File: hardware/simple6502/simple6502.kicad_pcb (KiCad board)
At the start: 2 copper layers, 100 x 100 mm, 41 parts, among them J1 ~{VP}, J2 CLK SEL, J3 RESET, J4 GND, J5 POWER 5V, J6 AUX 5VDC, SW1 RESET, SW2 POWER, T1 DS1813-10+, U1 W65C02SxP, U2 RAM 62256, U3 ROM 28C256, U4 74LS30, U5 74HCT00, U6 74HC138, U7 74HCT273, X1 ACO-1MHz

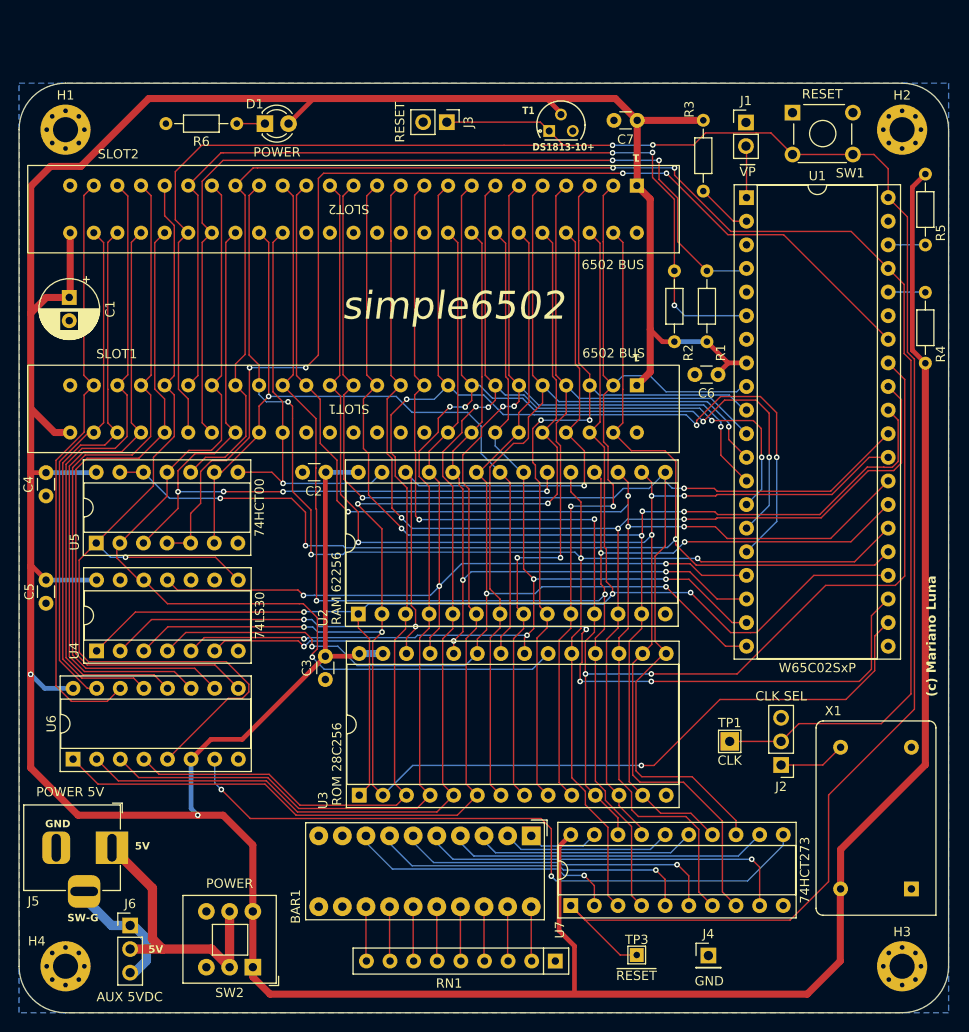
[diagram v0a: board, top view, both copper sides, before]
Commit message: new all in one design with ACIA 68B50
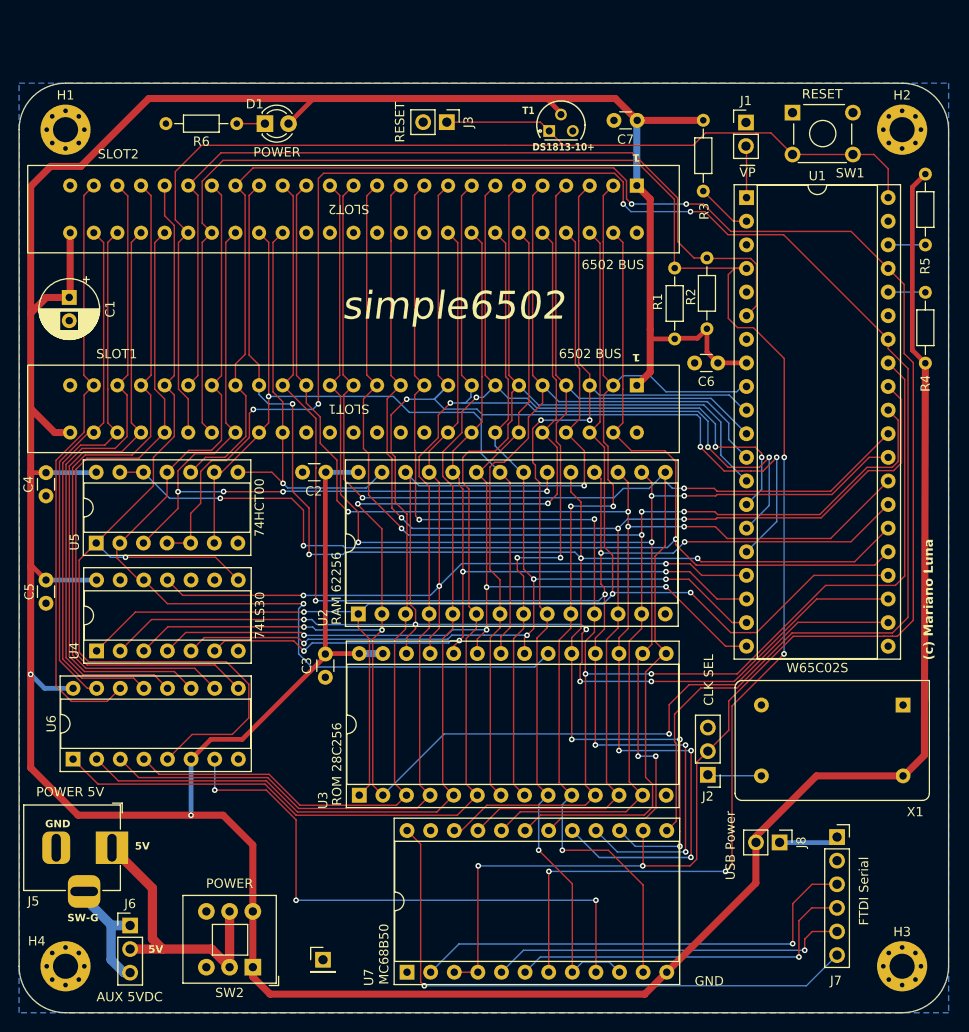
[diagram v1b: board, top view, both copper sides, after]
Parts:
- removed BAR1: HDSP-4850_2, Display:HDSP-4850
- removed RN1: R_Network08_US, Resistor_THT:R_Array_SIP9
- removed TP1: CLK, TestPoint:TestPoint_THTPad_2.0x2.0mm_Drill1.0mm
- removed TP3: ~{RESET}, TestPoint:TestPoint_THTPad_1.5x1.5mm_Drill0.7mm
- added J7: FTDI Serial, Connector_PinSocket_2.54mm:PinSocket_1x06_P2.54mm_Vertical, F.Cu at (138.0, 131.1)
- added J8: USB Power, Connector_PinHeader_2.54mm:PinHeader_1x02_P2.54mm_Vertical, F.Cu at (131.8, 131.7)
- U1: value W65C02SxP -> W65C02S
- U7: value 74HCT273 -> MC68B50; footprint Package_DIP:DIP-20_W7.62mm_Socket -> Package_DIP:DIP-24_W15.24mm_Socket
- moved J4 41.5 mm to (82.7, 144.3)
- moved X1 19.8 mm to (145.1, 116.9), turned to 180 degrees
- moved U7 19.0 mm to (91.7, 145.6)
- moved J2 7.95 mm to (124.1, 124.4)
- moved R2 3.77 mm to (124.0, 68.8)
- moved R1 3.48 mm to (120.5, 69.9)
- moved C6 1.25 mm to (125.2, 80.1)
- moved C3 0.24 mm to (83.0, 111.4)
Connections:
- U7 pad 1: ~{RESET} -> GND
- U7 pad 10: GND -> A1
- U7 pad 11: ~{IO_08} -> A0
- U7 pad 12: /Power and support/L3 -> VCC
- U7 pad 13: D3 -> R~{W}
- U7 pad 14: D2 -> CLK
- U7 pad 15: /Power and support/L2 -> D7
- U7 pad 16: /Power and support/L1 -> D6
- U7 pad 17: D1 -> D5
- U7 pad 18: D0 -> D4
- U7 pad 19: /Power and support/L0 -> D3
- U7 pad 2: /Power and support/L7 -> RXD
- U7 pad 20: VCC -> D2
- U7 pad 3: D7 -> CLK
- U7 pad 4: D6 -> CLK
- U7 pad 5: /Power and support/L6 -> ~{RTS}
- U7 pad 6: /Power and support/L5 -> TXD
- U7 pad 7: D5 -> ~{IRQ}
- U7 pad 8: D4 -> A1
- U7 pad 9: /Power and support/L4 -> ~{IO_08}
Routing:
- net ~{RESET}: track 244.8 -> 126.9 mm, vias 2 -> 0
- net ~{IRQ}: track 96.8 -> 199.7 mm, vias 2 -> 4
- net R~{W}: track 120.9 -> 195.7 mm
- net ~{CTS}: track 0.00 -> 63.2 mm, vias 0 -> 1
- net CLK: track 180.2 -> 235.1 mm, vias 2 -> 4
- net RXD: track 0.00 -> 50.4 mm, vias 0 -> 1
- net /Power and support/L4: track 40.7 -> 0.00 mm, vias 1 -> 0
- net TXD: track 0.00 -> 38.7 mm, vias 0 -> 1
- net ~{RTS}: track 0.00 -> 38.6 mm, vias 0 -> 1
- net /Power and support/L5: track 35.0 -> 0.00 mm, vias 1 -> 0
- net /Power and support/L6: track 34.9 -> 0.00 mm, vias 1 -> 0
- net /Power and support/L3: track 34.5 -> 0.00 mm
- net /Power and support/L7: track 29.4 -> 0.00 mm, vias 1 -> 0
- net A1: track 91.7 -> 118.7 mm, vias 2 -> 3
- net A0: track 88.7 -> 114.7 mm, vias 2 -> 3
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
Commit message: Corrected 6502 Bus pinout - re-routed
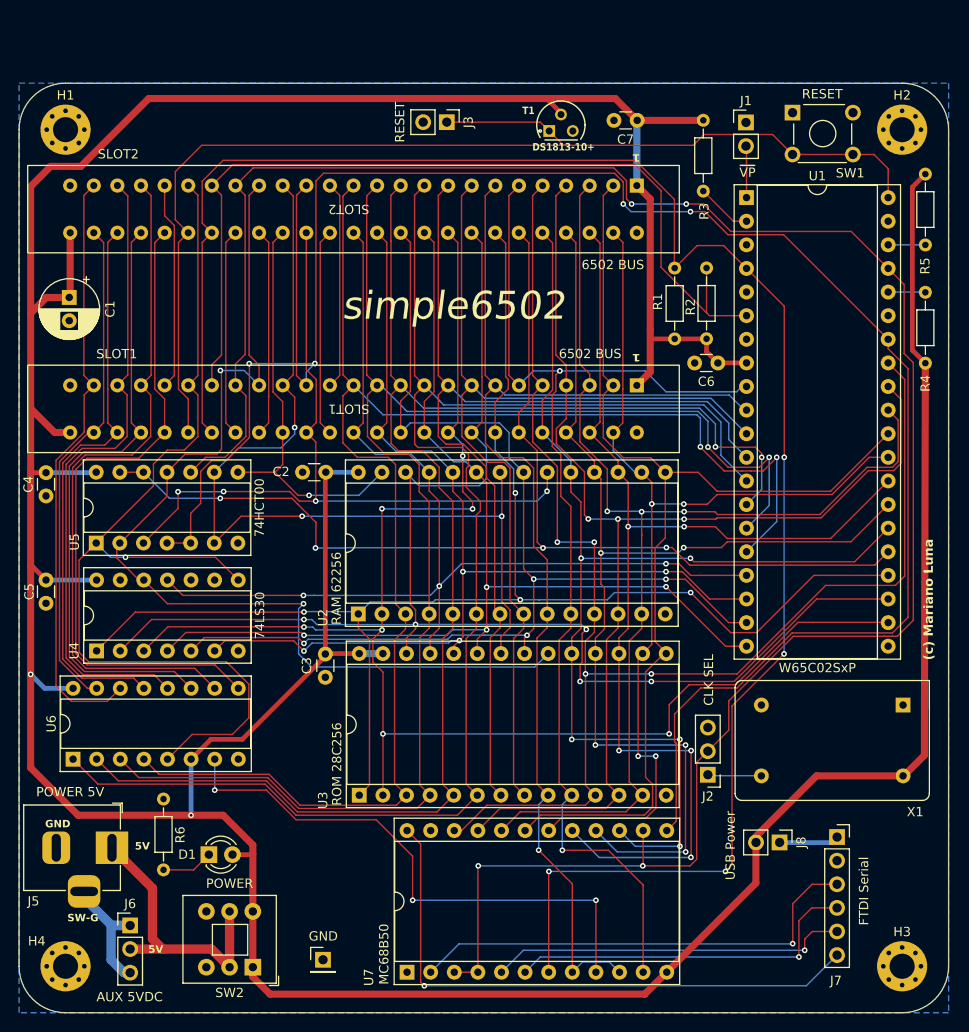
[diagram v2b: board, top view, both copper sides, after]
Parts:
- U1: value W65C02S -> W65C02SxP
- moved R6 80.7 mm to (65.5, 134.6), turned to 90 degrees
- moved D1 78.9 mm to (70.4, 133.0)
- moved R2 1.08 mm to (124.0, 69.9)
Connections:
- SLOT1 pad 10: D0 -> A4
- SLOT1 pad 11: D1 -> A5
- SLOT1 pad 12: D2 -> A6
- SLOT1 pad 13: D3 -> A7
- SLOT1 pad 14: D4 -> GND
- SLOT1 pad 15: D5 -> R~{W}
- SLOT1 pad 16: D6 -> ~{RD}
- SLOT1 pad 17: D7 -> ~{ROM_CS}
- SLOT1 pad 19: ~{ROM_CS} -> ~{NMI}
- SLOT1 pad 2: A0 -> D3
- SLOT1 pad 20: ~{NMI} -> ~{IO_CS}
- SLOT1 pad 21: ~{IO_CS} -> ~{IO_NC}
- SLOT1 pad 3: A1 -> D2
- SLOT1 pad 33: ~{RAM_CS} -> NC33
- SLOT1 pad 34: ~{RD} -> NC34
- SLOT1 pad 36: unconnected-(SLOT1-Pin_36-Pad36) -> ~{RAM_CS}
- SLOT1 pad 37: unconnected-(SLOT1-Pin_37-Pad37) -> GND
- SLOT1 pad 38: unconnected-(SLOT1-Pin_38-Pad38) -> A8
- SLOT1 pad 39: GND -> A9
- SLOT1 pad 4: A2 -> D1
- SLOT1 pad 40: unconnected-(SLOT1-Pin_40-Pad40) -> A10
- SLOT1 pad 41: unconnected-(SLOT1-Pin_41-Pad41) -> A11
- SLOT1 pad 42: A8 -> A12
- SLOT1 pad 43: A9 -> A13
- SLOT1 pad 44: A10 -> A14
- SLOT1 pad 45: A11 -> A15
- SLOT1 pad 46: A12 -> D7
- SLOT1 pad 47: A13 -> D6
- SLOT1 pad 48: A14 -> D5
- SLOT1 pad 49: A15 -> D4
- SLOT1 pad 5: A3 -> D0
- SLOT1 pad 6: A4 -> A0
- SLOT1 pad 7: A5 -> A1
- SLOT1 pad 8: A6 -> A2
- SLOT1 pad 9: A7 -> A3
- SLOT2 pad 10: D0 -> A4
- SLOT2 pad 11: D1 -> A5
- SLOT2 pad 12: D2 -> A6
- SLOT2 pad 13: D3 -> A7
- SLOT2 pad 14: D4 -> GND
- SLOT2 pad 15: D5 -> R~{W}
- SLOT2 pad 16: D6 -> ~{RD}
- SLOT2 pad 17: D7 -> ~{ROM_CS}
- SLOT2 pad 19: ~{ROM_CS} -> ~{NMI}
- SLOT2 pad 2: A0 -> D3
- SLOT2 pad 20: ~{NMI} -> ~{IO_CS}
- SLOT2 pad 21: ~{IO_CS} -> ~{IO_NC}
- SLOT2 pad 3: A1 -> D2
- SLOT2 pad 33: ~{RAM_CS} -> NC33
- SLOT2 pad 34: ~{RD} -> NC34
- SLOT2 pad 36: unconnected-(SLOT2-Pin_36-Pad36) -> ~{RAM_CS}
- SLOT2 pad 37: unconnected-(SLOT2-Pin_37-Pad37) -> GND
- SLOT2 pad 38: unconnected-(SLOT2-Pin_38-Pad38) -> A8
- SLOT2 pad 39: GND -> A9
- SLOT2 pad 4: A2 -> D1
- SLOT2 pad 40: unconnected-(SLOT2-Pin_40-Pad40) -> A10
- SLOT2 pad 41: unconnected-(SLOT2-Pin_41-Pad41) -> A11
- SLOT2 pad 42: A8 -> A12
- SLOT2 pad 43: A9 -> A13
- SLOT2 pad 44: A10 -> A14
- SLOT2 pad 45: A11 -> A15
- SLOT2 pad 46: A12 -> D7
- SLOT2 pad 47: A13 -> D6
- SLOT2 pad 48: A14 -> D5
- SLOT2 pad 49: A15 -> D4
- SLOT2 pad 5: A3 -> D0
- SLOT2 pad 6: A4 -> A0
- SLOT2 pad 7: A5 -> A1
- SLOT2 pad 8: A6 -> A2
- SLOT2 pad 9: A7 -> A3
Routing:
- net D6: track 173.6 -> 123.0 mm, vias 7 -> 5
- net D7: track 169.3 -> 122.6 mm, vias 7 -> 5
- net GND: track 0.00 -> 44.7 mm
- net D4: track 150.9 -> 107.5 mm, vias 6 -> 4
- net D5: track 163.0 -> 123.1 mm, vias 7 -> 5
- net D3: track 150.5 -> 117.2 mm, vias 2 -> 0
- net D2: track 151.4 -> 125.8 mm, vias 4 -> 3
- net R~{W}: track 195.7 -> 221.2 mm
- net ~{IO_NC}: track 0.00 -> 22.4 mm
- net NC34: track 0.00 -> 22.4 mm
- net NC33: track 0.00 -> 22.4 mm
- net D1: track 150.4 -> 131.2 mm
- net A12: track 175.9 -> 161.3 mm, vias 5 -> 7
- net D0: track 166.0 -> 152.0 mm
- net A4: track 149.9 -> 161.8 mm
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
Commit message: PCB ready DRC passed
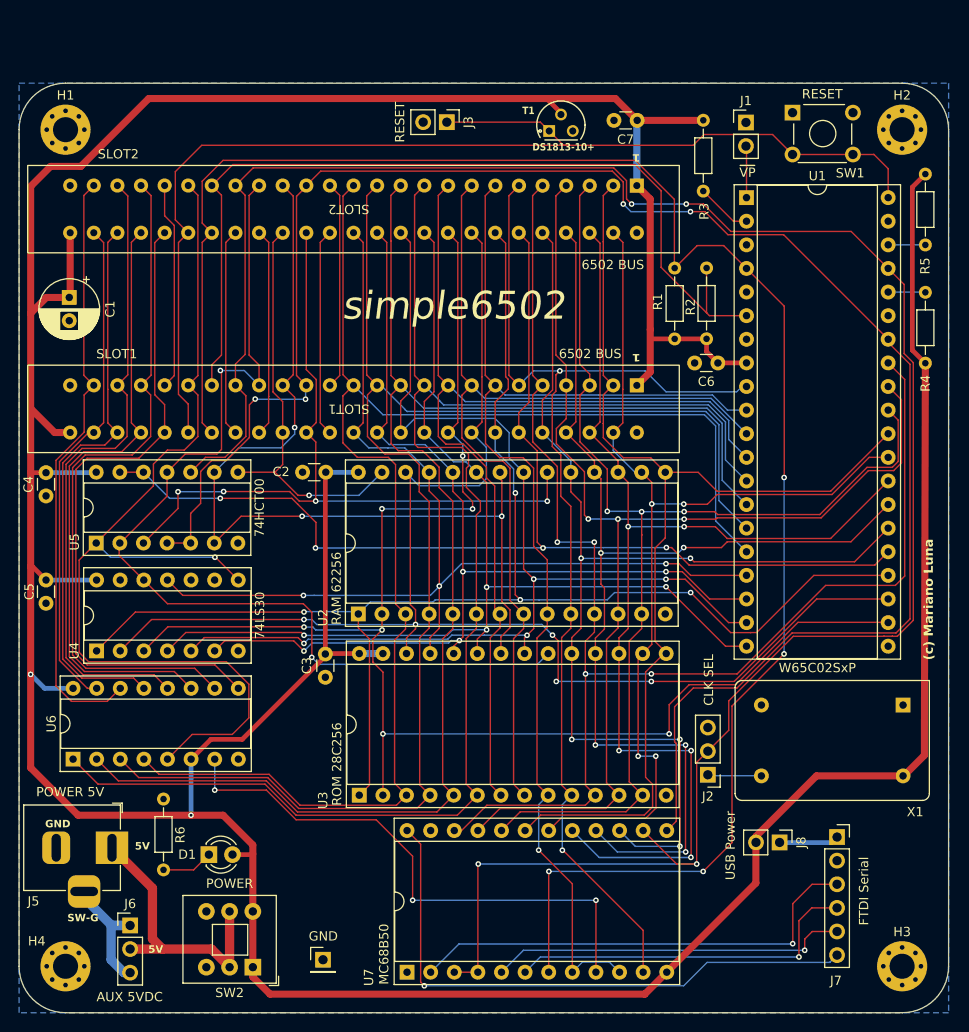
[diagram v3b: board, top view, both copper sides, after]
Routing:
- net R~{W}: track 221.2 -> 197.4 mm
- net A7: track 166.8 -> 159.2 mm, vias 2 -> 0
- net A6: track 164.8 -> 159.1 mm, vias 2 -> 0
- net CLK: track 235.0 -> 238.8 mm
- net A5: track 163.1 -> 159.7 mm, vias 2 -> 0
- net A0: track 122.2 -> 119.1 mm
- net ~{ROM_CS}: track 109.9 -> 108.1 mm
- net ~{IRQ}: track 198.0 -> 196.6 mm
- net A13: track 152.7 -> 151.3 mm
- net ~{RAM_CS}: track 79.9 -> 80.5 mm

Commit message: Updated VCC routing
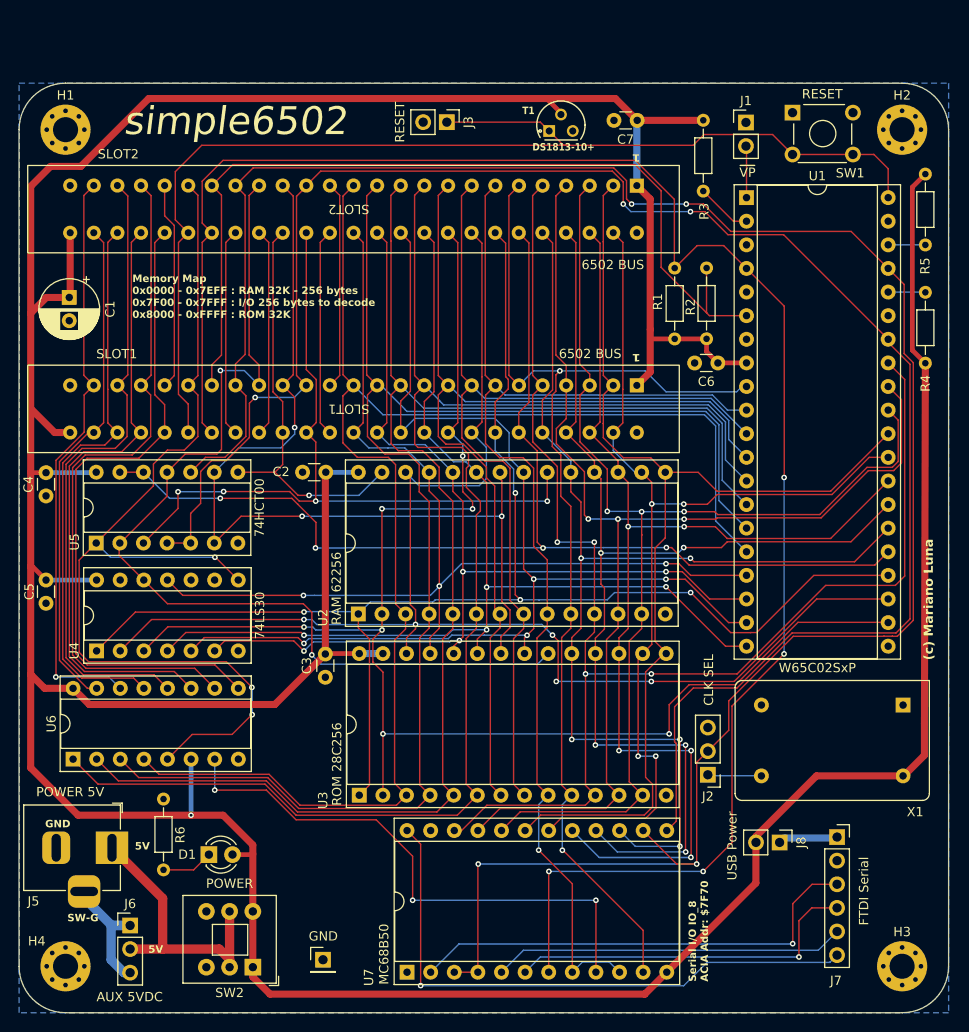
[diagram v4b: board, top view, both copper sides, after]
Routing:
- net VCC: track 473.3 -> 484.2 mm, vias 2 -> 1
- net ~{IO_02}: track 64.6 -> 62.9 mm, vias 0 -> 1
- net ~{RTS}: track 38.6 -> 37.9 mm, vias 1 -> 0
- net R~{W}: track 197.4 -> 196.8 mm, vias 4 -> 3
- net ~{IO_CS}: track 108.3 -> 108.6 mm, vias 1 -> 3
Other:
- board text added: "Memory Map 0x0000 - 0x7EFF : RAM 32K - 256 bytes 0x7F00 - 0x7FFF : I/O 256 bytes to decode 0x8000 - 0xFFFF : ROM 32K"
- board text added: "Serial I/O IO_8 ACIA Addr: $7F70"

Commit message: add the 40 pin header
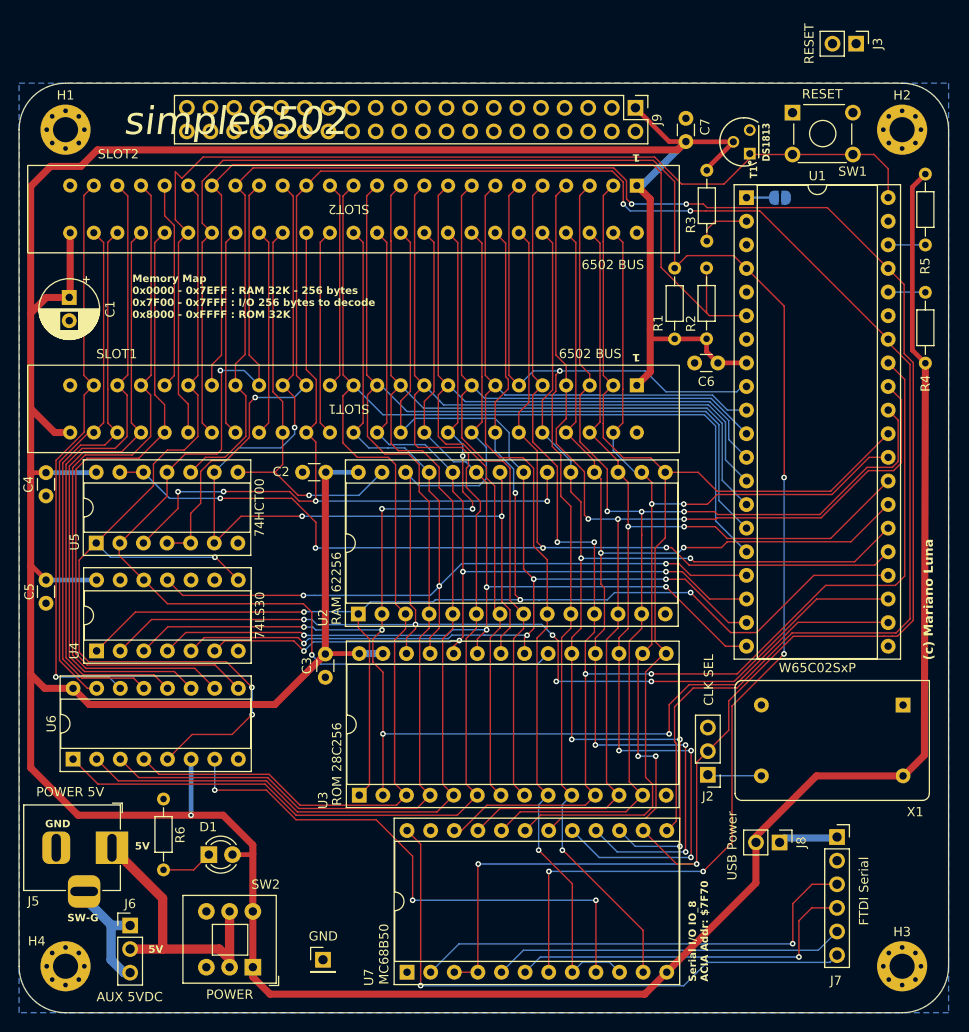
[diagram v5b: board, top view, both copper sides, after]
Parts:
- added J9: Expansion Port, Connector_PinHeader_2.54mm:PinHeader_2x20_P2.54mm_Vertical, F.Cu at (116.3, 52.6)
- J1: footprint Connector_PinHeader_2.54mm:PinHeader_1x02_P2.54mm_Vertical -> Jumper:SolderJumper-2_P1.3mm_Open_RoundedPad1.0x1.5mm; moved to B.Cu
- T1: value DS1813-10+ -> DS1813
- moved J3 44.8 mm to (140.1, 45.8)
- moved T1 17.8 mm to (127.3, 55.0), turned to 90 degrees
- moved J1 8.88 mm to (131.9, 62.3), turned to 180 degrees
- moved C7 5.71 mm to (121.7, 56.3), turned to 90 degrees
- moved R3 5.39 mm to (124.0, 67.0)
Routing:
- net ~{RESET}: track 126.4 -> 114.1 mm
- net VCC: track 484.2 -> 491.4 mm
- net /~{VP}: track 5.57 -> 2.95 mm
- net ~{NMI}: track 97.2 -> 98.3 mm
